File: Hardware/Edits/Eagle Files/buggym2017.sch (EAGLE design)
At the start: 6 parts, among them IC1-NOR 4001N, IC2-OR 4075N, IC3 BCC, IC4 L293E

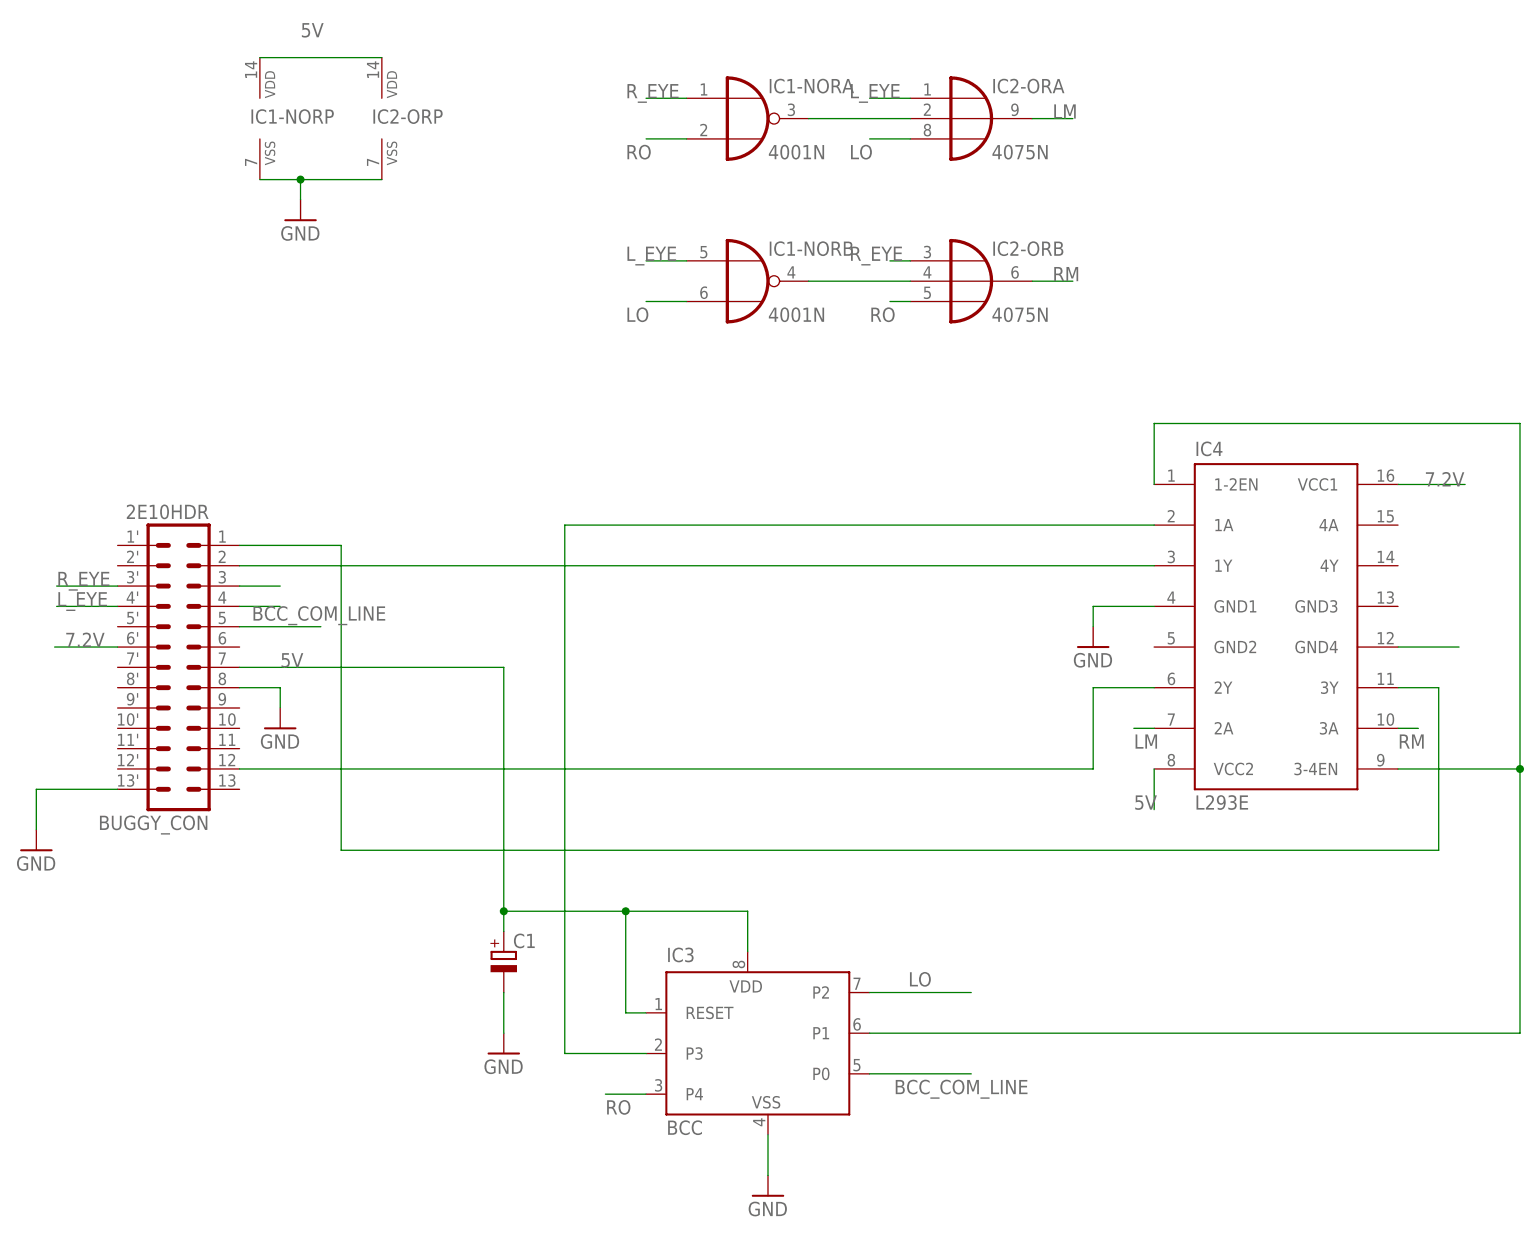
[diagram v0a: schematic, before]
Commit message: Work done in Hardware Lab 5
Finished schematic and new Arduino Sketch, blink without delay
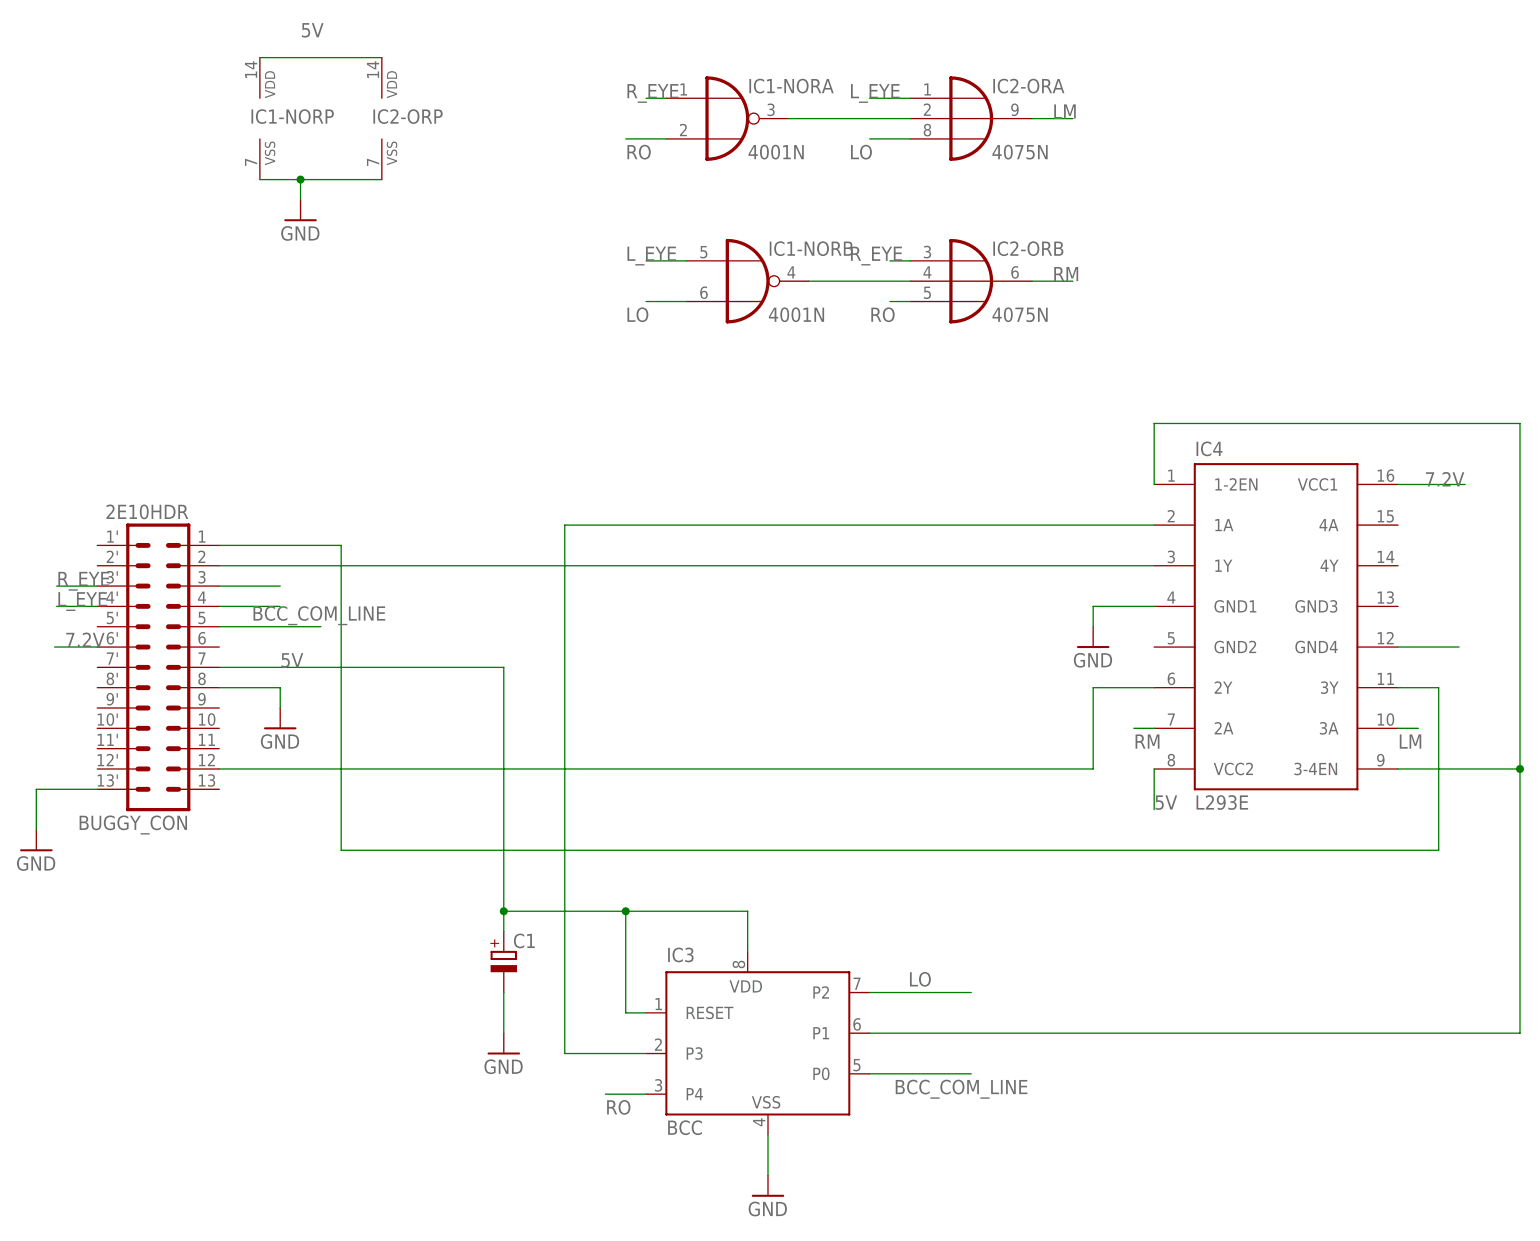
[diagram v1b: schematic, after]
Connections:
- net LM: now also IC4.3A; no longer IC4.2A
- net RM: now also IC4.2A; no longer IC4.3A
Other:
- moved on the sheet: BUGGY_CON, IC1-NORA
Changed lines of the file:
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@@
 <?xml version="1.0" encoding="utf-8"?>
 <!DOCTYPE eagle SYSTEM "eagle.dtd">
-<eagle version="8.0.0">
+<eagle version="7.7.0">
 <drawing>
 <settings>
@@
 <instance part="GND7" gate="1" x="-7.62" y="-25.4"/>
 <instance part="FRAME1" gate="G$1" x="-93.98" y="-60.96"/>
-<instance part="BUGGY_CON" gate="G$1" x="-48.26" y="22.86" rot="R180"/>
+<instance part="BUGGY_CON" gate="G$1" x="-50.8" y="22.86" rot="R180"/>
 <instance part="GND1" gate="1" x="-35.56" y="15.24"/>
 <instance part="GND3" gate="1" x="-66.04" y="0"/>
-<instance part="IC1-NOR" gate="A" x="22.86" y="91.44"/>
+<instance part="IC1-NOR" gate="A" x="20.32" y="91.44"/>
 <instance part="IC1-NOR" gate="B" x="22.86" y="71.12"/>
 <instance part="IC2-OR" gate="A" x="50.8" y="91.44"/>
@@
 <segment>
 <pinref part="BUGGY_CON" gate="G$1" pin="6'"/>
-<wire x1="-55.88" y1="25.4" x2="-63.754" y2="25.4" width="0.1524" layer="91"/>
+<wire x1="-58.42" y1="25.4" x2="-63.754" y2="25.4" width="0.1524" layer="91"/>
 <label x="-62.484" y="25.4" size="1.778" layer="95"/>
 </segment>
@@
 <wire x1="73.66" y1="5.08" x2="73.66" y2="10.16" width="0.1524" layer="91"/>
 <pinref part="IC4" gate="G$1" pin="VCC2"/>
-<label x="71.12" y="5.08" size="1.778" layer="95"/>
+<label x="73.66" y="5.08" size="1.778" layer="95"/>
 </segment>
 <segment>
@@
 <pinref part="BUGGY_CON" gate="G$1" pin="7"/>
 <label x="-35.56" y="22.86" size="1.778" layer="95"/>
-<wire x1="-7.62" y1="22.86" x2="-40.64" y2="22.86" width="0.1524" layer="91"/>
+<wire x1="-7.62" y1="22.86" x2="-43.18" y2="22.86" width="0.1524" layer="91"/>
 </segment>
 <segment>
@@
 <pinref part="BUGGY_CON" gate="G$1" pin="8"/>
 <wire x1="-35.56" y1="17.78" x2="-35.56" y2="20.32" width="0.1524" layer="91"/>
-<wire x1="-35.56" y1="20.32" x2="-40.64" y2="20.32" width="0.1524" layer="91"/>
+<wire x1="-35.56" y1="20.32" x2="-43.18" y2="20.32" width="0.1524" layer="91"/>
 </segment>
 <segment>
@@
 <wire x1="-66.04" y1="2.54" x2="-66.04" y2="7.62" width="0.1524" layer="91"/>
 <pinref part="BUGGY_CON" gate="G$1" pin="13'"/>
-<wire x1="-66.04" y1="7.62" x2="-55.88" y2="7.62" width="0.1524" layer="91"/>
+<wire x1="-66.04" y1="7.62" x2="-58.42" y2="7.62" width="0.1524" layer="91"/>
 </segment>
 <segment>
@@
 <segment>
 <pinref part="IC1-NOR" gate="A" pin="I1"/>
-<wire x1="15.24" y1="88.9" x2="10.16" y2="88.9" width="0.1524" layer="91"/>
+<wire x1="12.7" y1="88.9" x2="7.62" y2="88.9" width="0.1524" layer="91"/>
 <label x="7.62" y="86.36" size="1.778" layer="95"/>
 </segment>
@@
 <segment>
 <pinref part="BUGGY_CON" gate="G$1" pin="3'"/>
-<wire x1="-55.88" y1="33.02" x2="-63.5" y2="33.02" width="0.1524" layer="91"/>
+<wire x1="-58.42" y1="33.02" x2="-63.5" y2="33.02" width="0.1524" layer="91"/>
 <label x="-63.5" y="33.02" size="1.778" layer="95"/>
 </segment>
 <segment>
 <pinref part="IC1-NOR" gate="A" pin="I0"/>
-<wire x1="15.24" y1="93.98" x2="10.16" y2="93.98" width="0.1524" layer="91"/>
+<wire x1="12.7" y1="93.98" x2="10.16" y2="93.98" width="0.1524" layer="91"/>
 <label x="7.62" y="93.98" size="1.778" layer="95"/>
 </segment>
 <segment>
 <pinref part="BUGGY_CON" gate="G$1" pin="3"/>
-<wire x1="-40.64" y1="33.02" x2="-35.56" y2="33.02" width="0.1524" layer="91"/>
+<wire x1="-43.18" y1="33.02" x2="-35.56" y2="33.02" width="0.1524" layer="91"/>
 </segment>
 <segment>
@@
 <segment>
 <pinref part="BUGGY_CON" gate="G$1" pin="4'"/>
-<wire x1="-55.88" y1="30.48" x2="-63.5" y2="30.48" width="0.1524" layer="91"/>
+<wire x1="-58.42" y1="30.48" x2="-63.5" y2="30.48" width="0.1524" layer="91"/>
 <label x="-63.5" y="30.48" size="1.778" layer="95"/>
 </segment>
@@
 <segment>
 <pinref part="BUGGY_CON" gate="G$1" pin="4"/>
-<wire x1="-40.64" y1="30.48" x2="-35.56" y2="30.48" width="0.1524" layer="91"/>
+<wire x1="-43.18" y1="30.48" x2="-35.56" y2="30.48" width="0.1524" layer="91"/>
 </segment>
 <segment>
@@
 <segment>
 <pinref part="BUGGY_CON" gate="G$1" pin="1"/>
-<wire x1="-40.64" y1="38.1" x2="-27.94" y2="38.1" width="0.1524" layer="91"/>
+<wire x1="-43.18" y1="38.1" x2="-27.94" y2="38.1" width="0.1524" layer="91"/>
 <wire x1="-27.94" y1="38.1" x2="-27.94" y2="0" width="0.1524" layer="91"/>
 <wire x1="-27.94" y1="0" x2="109.22" y2="0" width="0.1524" layer="91"/>
@@
 <wire x1="66.04" y1="20.32" x2="73.66" y2="20.32" width="0.1524" layer="91"/>
 <pinref part="BUGGY_CON" gate="G$1" pin="12"/>
-<wire x1="-40.64" y1="10.16" x2="66.04" y2="10.16" width="0.1524" layer="91"/>
+<wire x1="-43.18" y1="10.16" x2="66.04" y2="10.16" width="0.1524" layer="91"/>
 </segment>
 </net>
@@
 <pinref part="BUGGY_CON" gate="G$1" pin="2"/>
 <pinref part="IC4" gate="G$1" pin="1Y"/>
-<wire x1="-40.64" y1="35.56" x2="73.66" y2="35.56" width="0.1524" layer="91"/>
+<wire x1="-43.18" y1="35.56" x2="73.66" y2="35.56" width="0.1524" layer="91"/>
 </segment>
 </net>
@@
 <segment>
 <pinref part="BUGGY_CON" gate="G$1" pin="5"/>
-<wire x1="-40.64" y1="27.94" x2="-30.48" y2="27.94" width="0.1524" layer="91"/>
+<wire x1="-43.18" y1="27.94" x2="-30.48" y2="27.94" width="0.1524" layer="91"/>
 <label x="-39.116" y="28.702" size="1.778" layer="95"/>
 </segment>
@@
 <pinref part="IC1-NOR" gate="A" pin="O"/>
 <pinref part="IC2-OR" gate="A" pin="I1"/>
-<wire x1="30.48" y1="91.44" x2="43.18" y2="91.44" width="0.1524" layer="91"/>
+<wire x1="27.94" y1="91.44" x2="43.18" y2="91.44" width="0.1524" layer="91"/>
 </segment>
 </net>
@@
 </segment>
 <segment>
-<pinref part="IC4" gate="G$1" pin="2A"/>
-<wire x1="71.12" y1="15.24" x2="73.66" y2="15.24" width="0.1524" layer="91"/>
-<label x="71.12" y="12.7" size="1.778" layer="95"/>
+<pinref part="IC4" gate="G$1" pin="3A"/>
+<wire x1="104.14" y1="15.24" x2="106.68" y2="15.24" width="0.1524" layer="91"/>
+<label x="104.14" y="12.7" size="1.778" layer="95"/>
 </segment>
 </net>
@@
 </segment>
 <segment>
-<pinref part="IC4" gate="G$1" pin="3A"/>
-<wire x1="104.14" y1="15.24" x2="106.68" y2="15.24" width="0.1524" layer="91"/>
-<label x="104.14" y="12.7" size="1.778" layer="95"/>
-</segment>
-</net>
+<pinref part="IC4" gate="G$1" pin="2A"/>
+<wire x1="73.66" y1="15.24" x2="71.12" y2="15.24" width="0.1524" layer="91"/>
+<label x="71.12" y="12.7" size="1.778" layer="95"/>
+</segment>
+</net>
